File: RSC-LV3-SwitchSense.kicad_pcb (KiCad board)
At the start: 2 copper layers, 140 x 85 mm, 171 parts, among them J1 FTSH-105-01-L-DV-K-A, J10 Molex 43045-0400, J11 Molex 43045-0400, J12 Molex 43045-0400, J13 Molex 43045-0400, J14 Molex 43045-0400, J15 Molex 43045-0400, J16 Molex 43650-0200, J2 USB_C_Receptacle_USB2.0_16P, J3 Molex 43650-0500, J4 Molex 43650-0500, J5 Molex 43650-0200, J6 Molex 43045-0400, J7 Molex 43045-0400, J8 Molex 43045-0400, J9 Molex 43045-0400, Q1 AO3400A, Q10 AO3400A, Q2 AO3400A, Q3 AO3400A, Q4 AO3400A, Q5 AO3400A, Q6 AO3400A, Q7 AO3400A, Q8 AO3400A, Q9 AO3400A, U1 STM32G0B1CBTx, U2 TPS54302, U3 TLV74033PDBVR, U4 TJA1051T-3, U5 TJA1051T-3, Y1 Crystal_GND24, Y2 32.768 kHz 6pF

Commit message: silkscreen work
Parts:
- moved D2 0.25 mm to (99.0, 123.2)
- moved D3 0.25 mm to (99.0, 130.8)
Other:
- board text added: "STAT0"
- board text added: "STAT1"

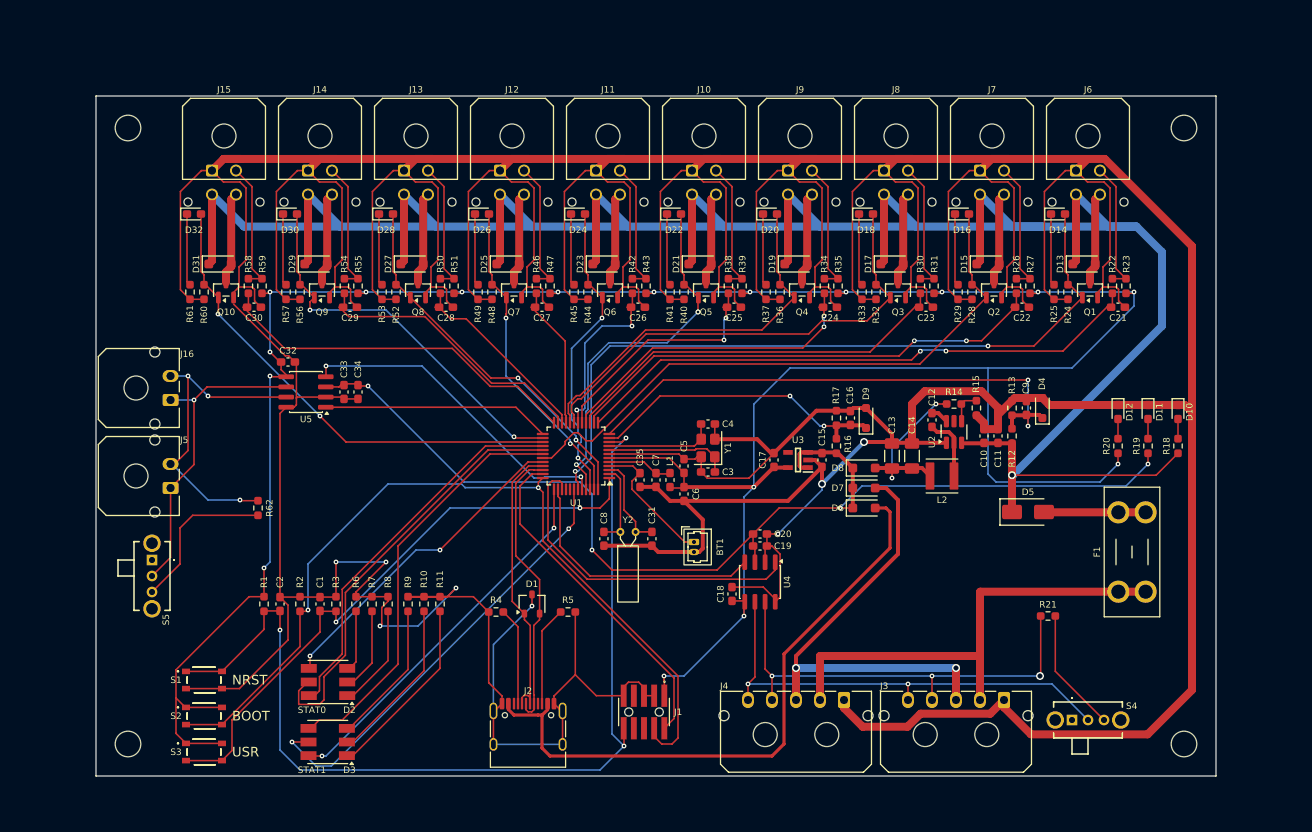
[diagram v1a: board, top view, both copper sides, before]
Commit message: more silkscreen and routing cleanup
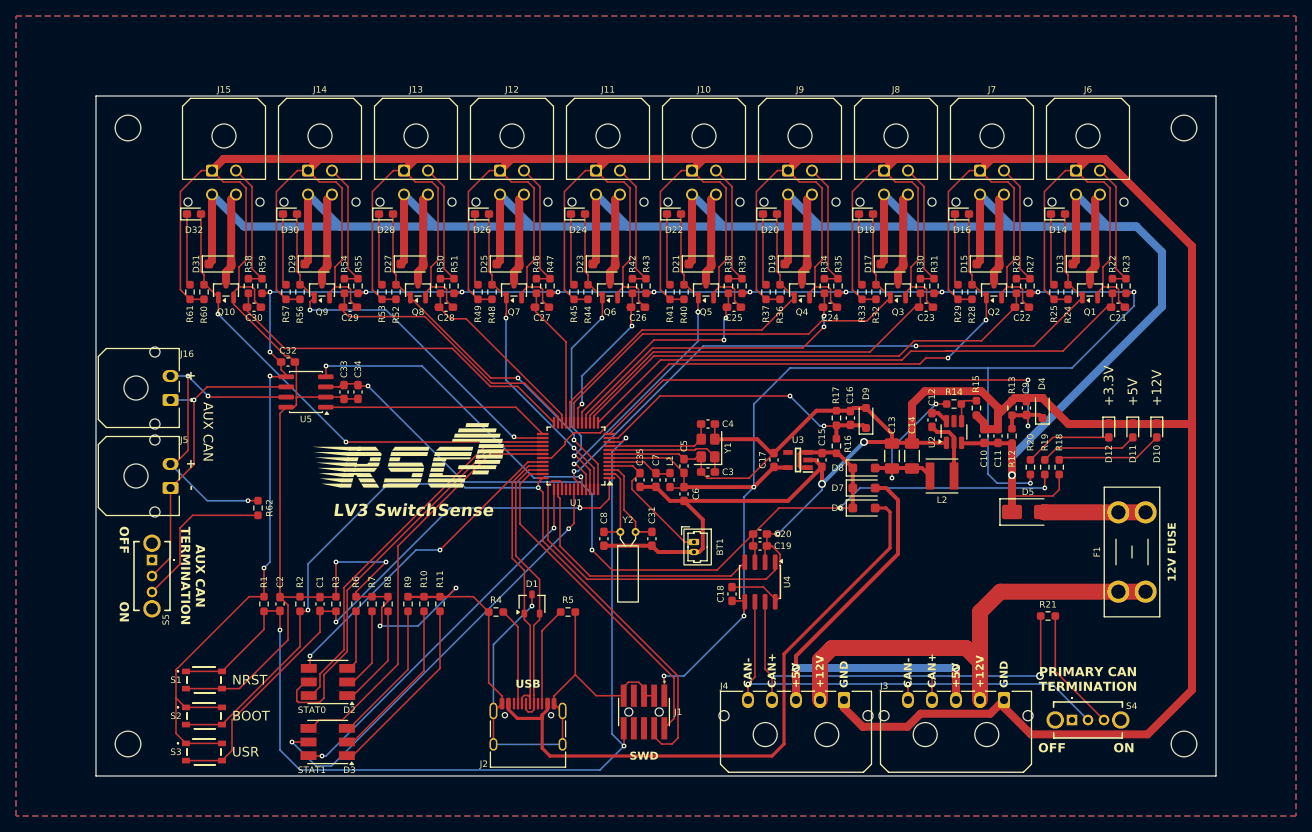
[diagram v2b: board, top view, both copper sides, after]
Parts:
- moved R18 15.1 mm to (190.4, 96.4)
- moved R19 13.2 mm to (188.6, 96.4)
- moved R20 11.3 mm to (186.8, 96.4)
- moved D10 3.51 mm to (202.6, 91.8)
- moved D11 2.98 mm to (199.6, 91.8)
- moved D12 2.57 mm to (196.6, 91.8)
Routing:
- net +12V: track 341.3 -> 327.4 mm
- net +5V: track 143.9 -> 130.1 mm
- net +3.3V: track 355.7 -> 343.6 mm
- net Net-(D10-A): track 2.46 -> 13.4 mm
- net Net-(D11-A): track 2.46 -> 12.2 mm
- net Net-(D12-A): track 2.46 -> 11.0 mm
- net OUT_1: track 93.0 -> 86.4 mm
- net OUT_5: track 46.7 -> 42.7 mm
- net IN_6: track 22.4 -> 19.6 mm
- net GND: track 1127.5 -> 1129.0 mm
- net IN_1: track 72.0 -> 72.9 mm, vias 2 -> 0
- net OUT_2: track 76.2 -> 77.0 mm, vias 0 -> 2
- net +12V_IN: track 59.7 -> 59.1 mm
- net +5V_USB: track 78.9 -> 79.5 mm
- net OUT_6: track 38.3 -> 38.8 mm
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- added copper zone on B.Cu, net GND
- added copper zone on F.Cu, net GND
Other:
- board text added: "+"
- board text added: "+12V"
- board text added: "+3.3V"
- board text added: "+5V"
- board text added: "-"
- board text added: "12V FUSE"
- board text added: "AUX CAN"
- board text added: "AUX CAN TERMINATION"
- board text added: "CAN+"
- board text added: "CAN-"
- board text added: "GND"
- board text added: "LV3 SwitchSense"
- board text added: "OFF"
- board text added: "ON"
- board text added: "PRIMARY CAN TERMINATION"
- board text added: "SWD"
- board text added: "USB"

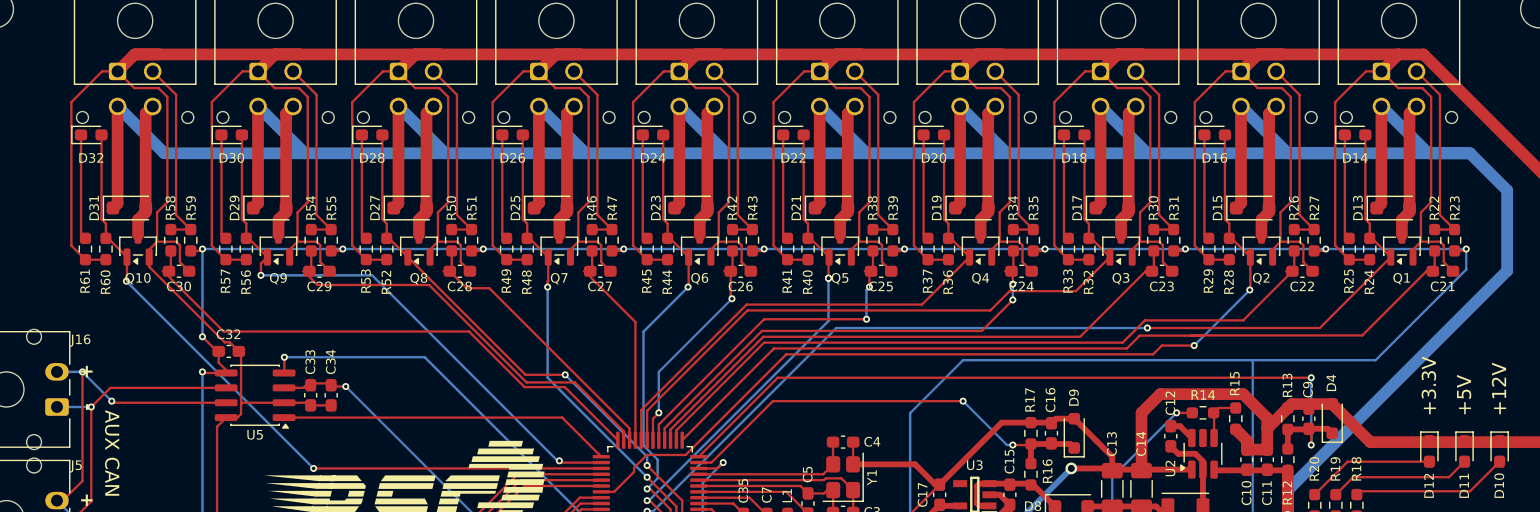
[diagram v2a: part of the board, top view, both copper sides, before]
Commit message: add zener diodes to inputs
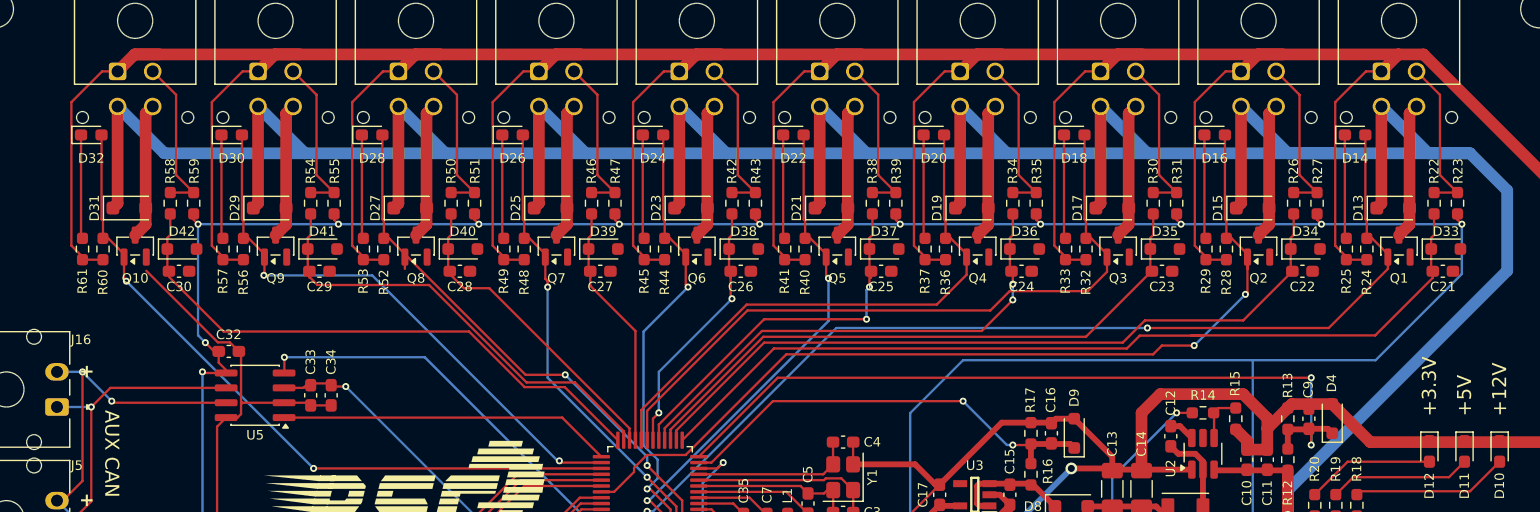
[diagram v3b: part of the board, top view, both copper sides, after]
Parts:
- added D33: D_Zener, Diode_SMD:D_SOD-323_HandSoldering, F.Cu at (198.0, 74.5)
- added D34: D_Zener, Diode_SMD:D_SOD-323_HandSoldering, F.Cu at (186.0, 74.5)
- added D35: D_Zener, Diode_SMD:D_SOD-323_HandSoldering, F.Cu at (174.0, 74.5)
- added D36: D_Zener, Diode_SMD:D_SOD-323_HandSoldering, F.Cu at (162.0, 74.5)
- added D37: D_Zener, Diode_SMD:D_SOD-323_HandSoldering, F.Cu at (150.0, 74.5)
- added D38: D_Zener, Diode_SMD:D_SOD-323_HandSoldering, F.Cu at (138.0, 74.5)
- added D39: D_Zener, Diode_SMD:D_SOD-323_HandSoldering, F.Cu at (126.0, 74.5)
- added D40: D_Zener, Diode_SMD:D_SOD-323_HandSoldering, F.Cu at (114.0, 74.5)
- added D41: D_Zener, Diode_SMD:D_SOD-323_HandSoldering, F.Cu at (102.0, 74.5)
- added D42: D_Zener, Diode_SMD:D_SOD-323_HandSoldering, F.Cu at (90.0, 74.5)
- moved R23 3.17 mm to (199.0, 70.6)
- moved R27 3.17 mm to (187.0, 70.6)
- moved R31 3.17 mm to (175.0, 70.6)
- moved R35 3.17 mm to (163.0, 70.6)
- moved R39 3.17 mm to (151.0, 70.6)
- moved R43 3.17 mm to (139.0, 70.6)
- moved R47 3.17 mm to (127.0, 70.6)
- moved R51 3.17 mm to (115.0, 70.6)
- moved R55 3.17 mm to (103.0, 70.6)
- moved R59 3.17 mm to (91.0, 70.6)
- moved R22 3.16 mm to (197.0, 70.6)
- moved R26 3.16 mm to (185.0, 70.6)
- moved R30 3.16 mm to (173.0, 70.6)
- moved R34 3.16 mm to (161.0, 70.6)
- moved R38 3.16 mm to (149.0, 70.6)
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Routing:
- net GND: track 1129.0 -> 884.9 mm
- net +3.3V: track 343.6 -> 347.7 mm
- net IN_7: track 17.9 -> 21.7 mm
- net IN_1: track 72.9 -> 76.5 mm
- net IN_9: track 35.4 -> 38.7 mm
- net IN_6: track 19.6 -> 22.9 mm
- net IN_5: track 29.2 -> 32.5 mm
- net IN_3: track 49.5 -> 52.7 mm
- net Net-(J15-Pin_2): track 16.6 -> 13.8 mm
- net Net-(J14-Pin_2): track 16.6 -> 13.8 mm
- net Net-(J13-Pin_2): track 16.6 -> 13.8 mm
- net Net-(J12-Pin_2): track 16.6 -> 13.8 mm
- net Net-(J9-Pin_2): track 16.6 -> 13.8 mm
- net Net-(J7-Pin_2): track 16.6 -> 13.8 mm
- net Net-(J6-Pin_2): track 16.6 -> 13.8 mm
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
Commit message: silkscreen tweaks
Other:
- board text added: "1"
- board text added: "10"
- board text added: "2"
- board text added: "3"
- board text added: "4"
- board text added: "5"
- board text added: "6"
- board text added: "7"
- board text added: "8"
- board text added: "9"
- board text added: "r0 • Jun 2026 • Cy Westbrook"

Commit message: add electrolytic capacitors and minor layout and silkscreen adjustments
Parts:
- added C36: 100u, Capacitor_THT:CP_Radial_D6.3mm_P2.50mm, F.Cu at (180.2, 105.8)
- added C37: 100u, Capacitor_THT:CP_Radial_D6.3mm_P2.50mm, F.Cu at (172.8, 105.8)
- moved J2 0.75 mm to (124.0, 130.8)
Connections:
- J2 pad SH: GND -> (no net)
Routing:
- net GND: track 884.9 -> 921.1 mm
- net +12V: track 327.1 -> 340.4 mm
- net USB+: track 35.9 -> 36.6 mm
- net USB-: track 36.0 -> 36.8 mm

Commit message: minor layout and silkscreen changes
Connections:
- J2 pad SH: (no net) -> GND
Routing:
- net OUT_8: track 48.3 -> 47.3 mm
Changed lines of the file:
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@@
 			(layers "*.Cu" "*.Mask")
 			(remove_unused_layers no)
+			(net "GND")
 		)
 		(pad "SH" thru_hole oval
@@
 			(layers "*.Cu" "*.Mask")
 			(remove_unused_layers no)
+			(net "GND")
 		)
 		(pad "SH" thru_hole oval
@@
 			(layers "*.Cu" "*.Mask")
 			(remove_unused_layers no)
+			(net "GND")
 		)
 		(pad "SH" thru_hole oval
@@
 			(layers "*.Cu" "*.Mask")
 			(remove_unused_layers no)
+			(net "GND")
 		)
 		(embedded_fonts no)
@@
 		)
 	)
+	(barcode
+		(at 91.5 113.5 0)
+		(layer "B.SilkS")
+		(size 15 15)
+		(text "https://cy2.me/pcb/rsc-lv3-switchsense-r0")
+		(text_height 1)
+		(type qr)
+		(ecc_level M)
+		(hide yes)
+		(knockout no)
+	)
 	(dimension
 		(type orthogonal)
@@
 		(width 0.2)
 		(layer "F.Cu")
-		(net "OUT_8")
-	)
-	(segment
-		(start 109.05 75.1875)
-		(end 109.05 76.2)
-		(width 0.2)
-		(layer "F.Cu")
